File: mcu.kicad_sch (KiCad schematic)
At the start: 124 parts, among them Q1 NMOS, Q2 NMOS, SW1 SW_Push, U1 PIC32CK1025GC01100-I/4SB, Y1 Crystal, Y2 Crystal

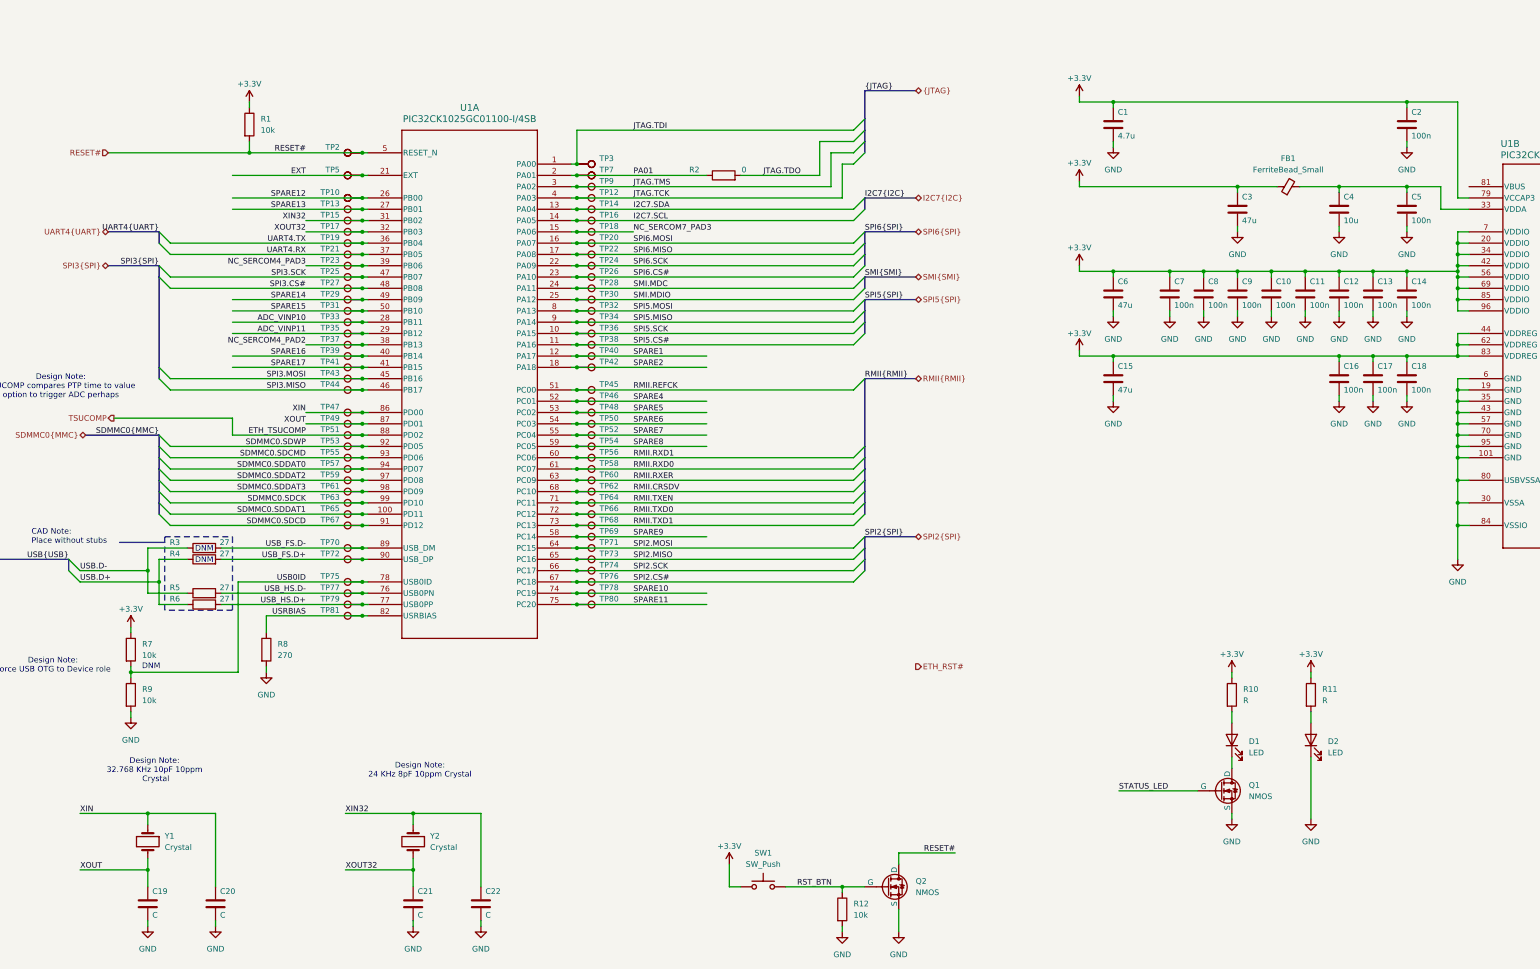
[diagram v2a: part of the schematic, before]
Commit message: changed to 4 layer, finished usb conn, added jtag conn, some other things
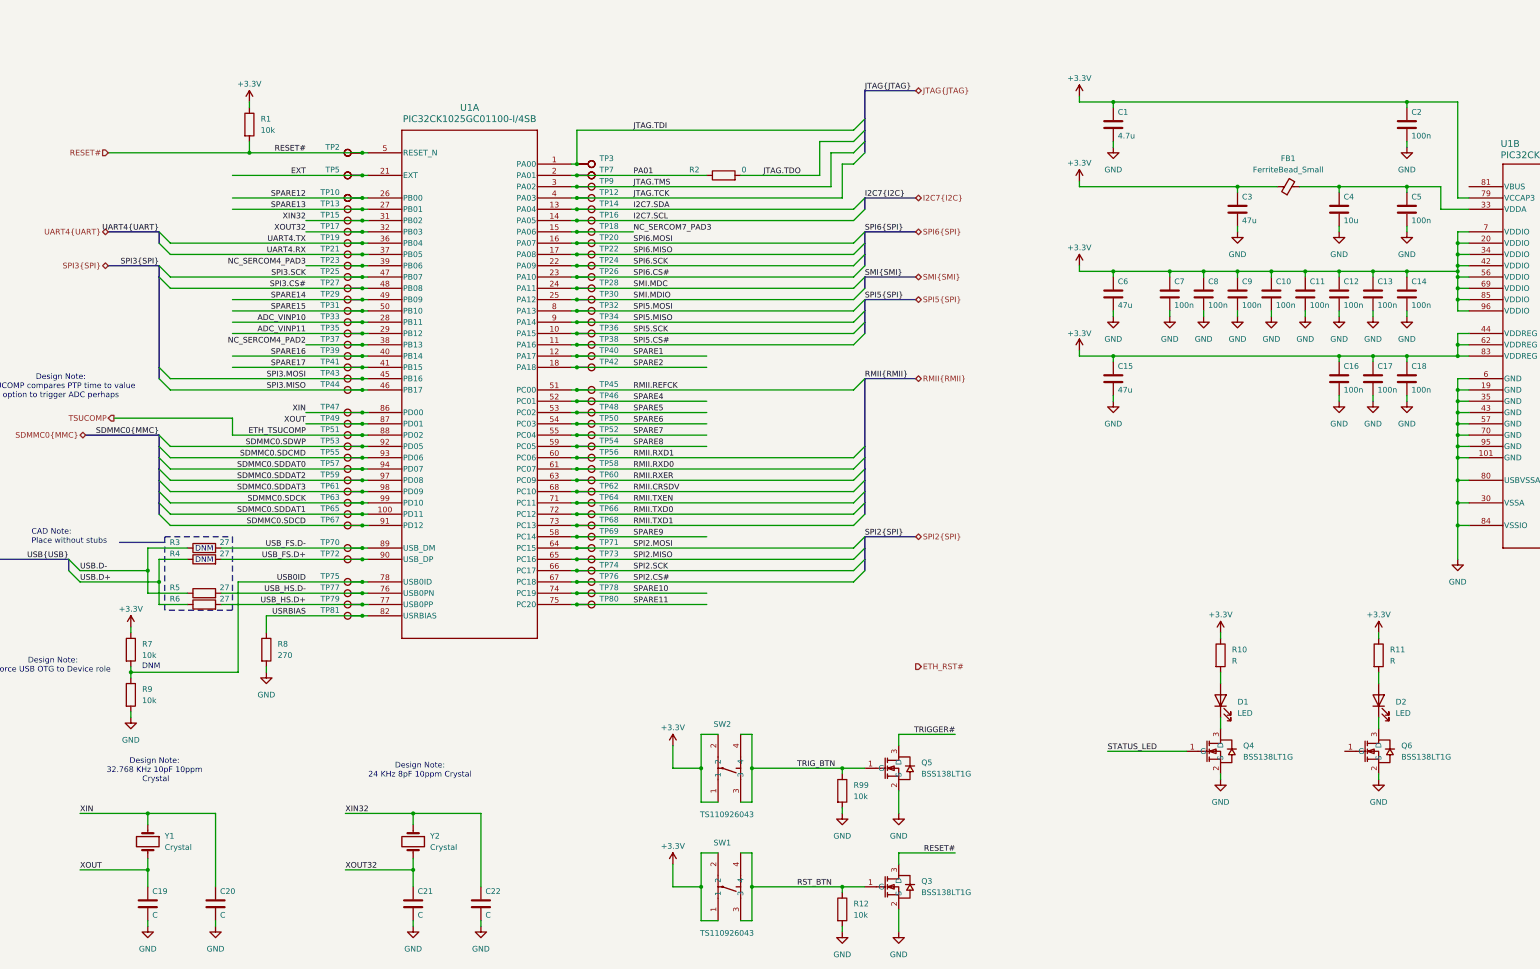
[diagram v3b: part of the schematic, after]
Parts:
- removed Q1, Q2: NMOS, symbol Simulation_SPICE:NMOS
- removed SW1: SW_Push, symbol Switch:SW_Push
- added Q3, Q4, Q5, Q6: BSS138LT1G, C82045:SOT-23-3_L2.9-W1.6-P1.90-LS2.8-BR, symbol C82045:BSS138LT1G
- added R99: 10k, Resistor_SMD:R_0402_1005Metric, symbol Device:R
- added SW1, SW2: TS110926043, C22375349:SW-SMD_4P-L4.5-W4.5-P3.00-LS7.5, symbol C22375349:TS110926043
- TP1, TP10, TP11, TP12, TP13, TP14, TP15, TP16, TP17, TP18, TP19, TP2, TP20, TP21, TP22, TP23, TP24, TP25, TP26, TP27, TP28, TP29, TP3, TP30, TP31, TP32, TP33, TP34, TP35, TP36, TP37, TP38, TP39, TP4, TP40, TP41, TP42, TP43, TP44, TP45, TP46, TP47, TP48, TP49, TP5, TP50, TP51, TP52, TP53, TP54, TP55, TP56, TP57, TP58, TP59, TP6, TP60, TP61, TP62, TP63, TP64, TP65, TP66, TP67, TP68, TP69, TP7, TP70, TP71, TP72, TP73, TP74, TP75, TP76, TP77, TP78, TP79, TP8, TP80, TP81, TP9: footprint (none) -> TestPoint:TestPoint_THTPad_D1.0mm_Drill0.5mm
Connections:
- net +3.3V: now also SW1.1, SW1.2, SW2.1, SW2.2
- net GND: now also Q3.2 (S), Q4.2 (S), Q5.2 (S), Q6.2 (S), R99.2; no longer D2.1 (K)
- net RESET#: now also Q3.3 (D)
- net RST_BTN: now also Q3.1 (G), SW1.3, SW1.4
- net STATUS_LED: now also Q4.1 (G)
- net at D1.1 (K): now also Q4.3 (D)
- new net: D2.1 (K), Q6.3 (D)
- new net TRIGGER#: Q5.3 (D)
- new net TRIG_BTN: Q5.1 (G), R99.1, SW2.3, SW2.4
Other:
- moved on the sheet: D1, D2, R10, R11

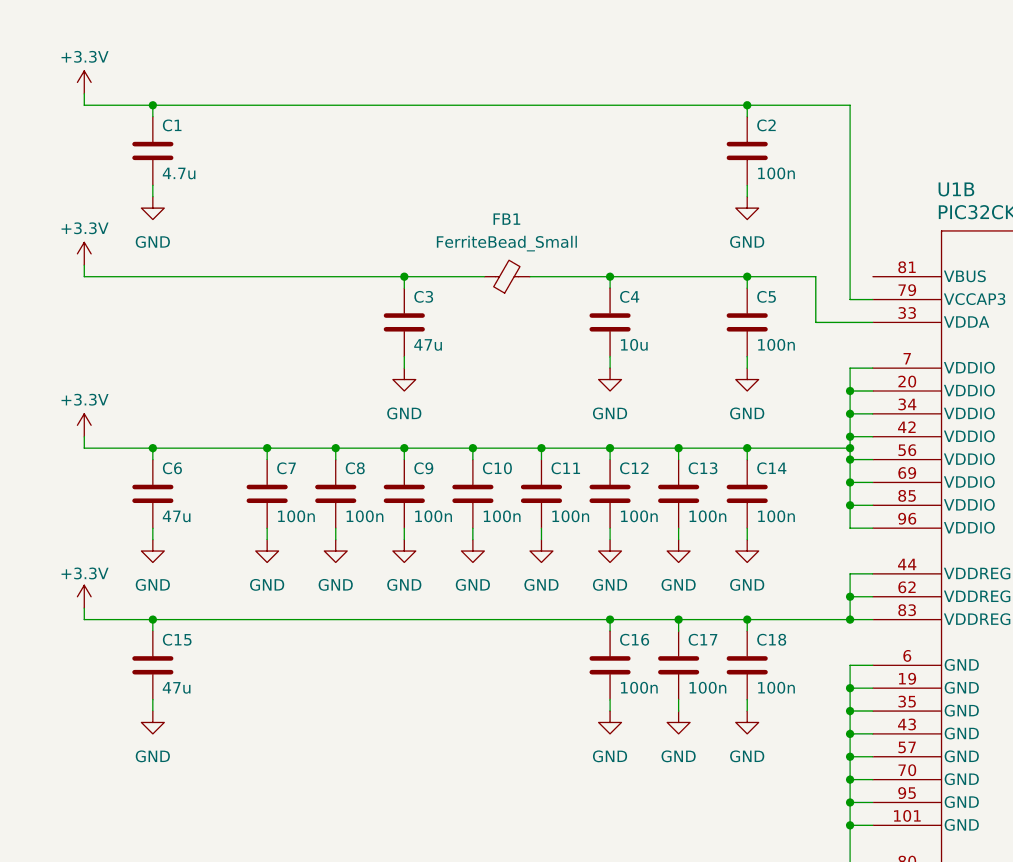
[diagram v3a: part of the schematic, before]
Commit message: did a bunch of bom matching to lcsc
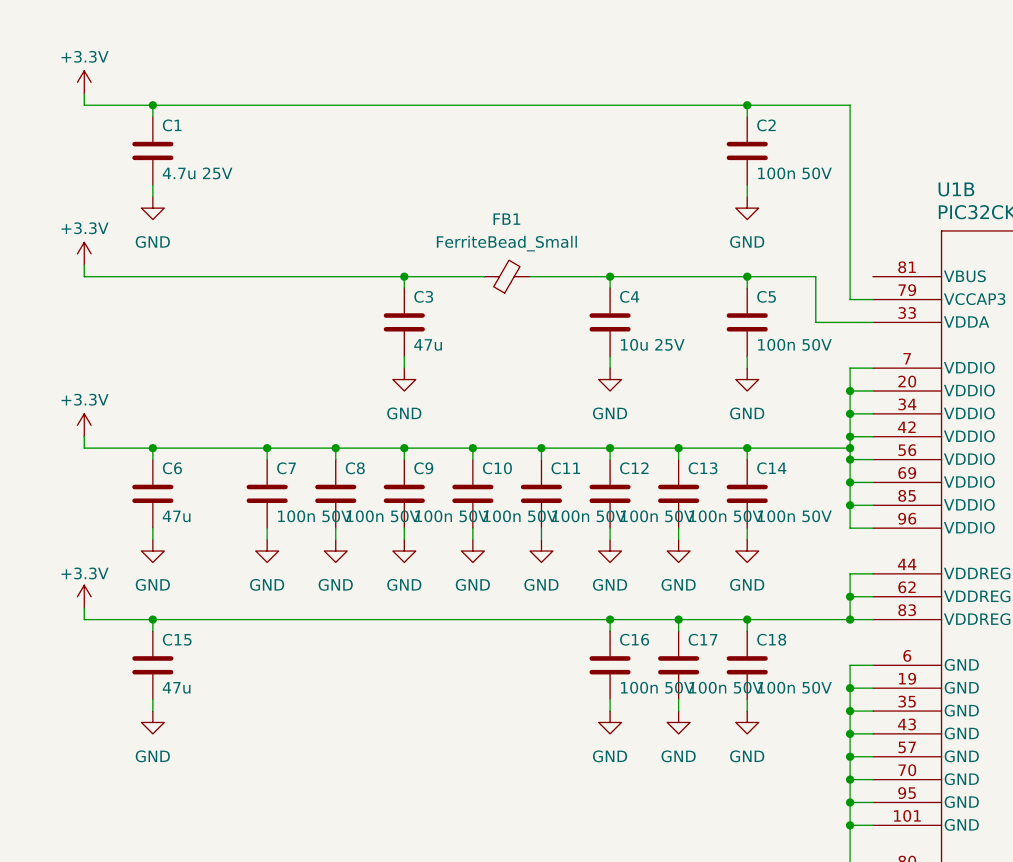
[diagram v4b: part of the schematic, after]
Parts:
- C1: value 4.7u -> 4.7u 25V; LCSC (none) -> C1779; LCSC Basic/Pref (none) -> x; LCSC Part (none) -> C1779
- C10, C11, C12, C13, C14, C16, C17, C18, C2, C5, C7, C8, C9: value 100n -> 100n 50V; LCSC (none) -> C307331; LCSC Basic/Pref (none) -> x; LCSC Part (none) -> C307331
- C15, C3, C6: footprint Capacitor_SMD:C_1210_3225Metric -> Capacitor_SMD:C_1206_3216Metric; LCSC (none) -> C96123; LCSC Basic/Pref (none) -> x; LCSC Part (none) -> C96123
- C4: value 10u -> 10u 25V; LCSC (none) -> C15850; LCSC Basic/Pref (none) -> x; LCSC Part (none) -> C15850
- R1, R12, R7, R9, R99: LCSC (none) -> C25744; LCSC Basic/Pref (none) -> x; LCSC Part (none) -> C25744
- R2: LCSC (none) -> C17168; LCSC Basic/Pref (none) -> x; LCSC Part (none) -> C17168
- R3, R4, R5, R6: footprint Resistor_SMD:R_0402_1005Metric -> Resistor_SMD:R_0603_1608Metric; LCSC (none) -> C25190; LCSC Basic/Pref (none) -> x; LCSC Part (none) -> C25190
- R8: footprint Resistor_SMD:R_0402_1005Metric -> Resistor_SMD:R_0603_1608Metric; LCSC (none) -> C22966; LCSC Basic/Pref (none) -> x; LCSC Part (none) -> C22966
- TP1, TP10, TP11, TP12, TP13, TP14, TP15, TP16, TP17, TP18, TP19, TP2, TP20, TP21, TP22, TP23, TP24, TP25, TP26, TP27, TP28, TP29, TP3, TP30, TP31, TP32, TP33, TP34, TP35, TP36, TP37, TP38, TP39, TP4, TP40, TP41, TP42, TP43, TP44, TP45, TP46, TP47, TP48, TP49, TP5, TP50, TP51, TP52, TP53, TP54, TP55, TP56, TP57, TP58, TP59, TP6, TP60, TP61, TP62, TP63, TP64, TP65, TP66, TP67, TP68, TP69, TP7, TP70, TP71, TP72, TP73, TP74, TP75, TP76, TP77, TP78, TP79, TP8, TP80, TP81, TP9: now left out of the parts list
- U1: LCSC missing (none) -> x

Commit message: bunch of stuff
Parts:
- removed Y1, Y2: Crystal, symbol Device:Crystal
- added X2: Q13FC1350000400, C32346:FC-135R_L3.2-W1.5, symbol C32346:Q13FC1350000400
- added X3: X322512MSB4SI, C9002:CRYSTAL-SMD_4P-L3.2-W2.5-BL, symbol C9002:X322512MSB4SI
- C19, C20: value C -> 33p; LCSC (none) -> C1562; LCSC Basic/Pref (none) -> x; LCSC Part (none) -> C1562
- C21, C22: value C -> 18p; LCSC (none) -> C1549; LCSC Basic/Pref (none) -> x; LCSC Part (none) -> C1549
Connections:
- net GND: now also X3.2 (GND), X3.4 (GND)
- net XIN: now also X3.3 (OSC2)
- net XIN32: now also X2.1
- net XOUT: now also X3.1 (OSC1)
- net XOUT32: now also X2.2
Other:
- note added: "Design Note: 12 MHz 20pF 10ppm Crystal"
- note added: "Design Note: 32.768 KHz 12.5pF 20ppm Crystal"
- note removed: "Design Note: 24 KHz 8pF 10ppm Crystal"
- note removed: "Design Note: 32.768 KHz 10pF 10ppm Crystal"
- moved on the sheet: C19, C20
